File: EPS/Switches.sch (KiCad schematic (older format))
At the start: 13 parts, among them Q13 PMOS_IN, Q14 Q_NMOS_GSD, Q15 PMOS_IN, Q16 PMOS_OUT1, Q17 PMOS_OUT2, Q18 NMOS_MCU

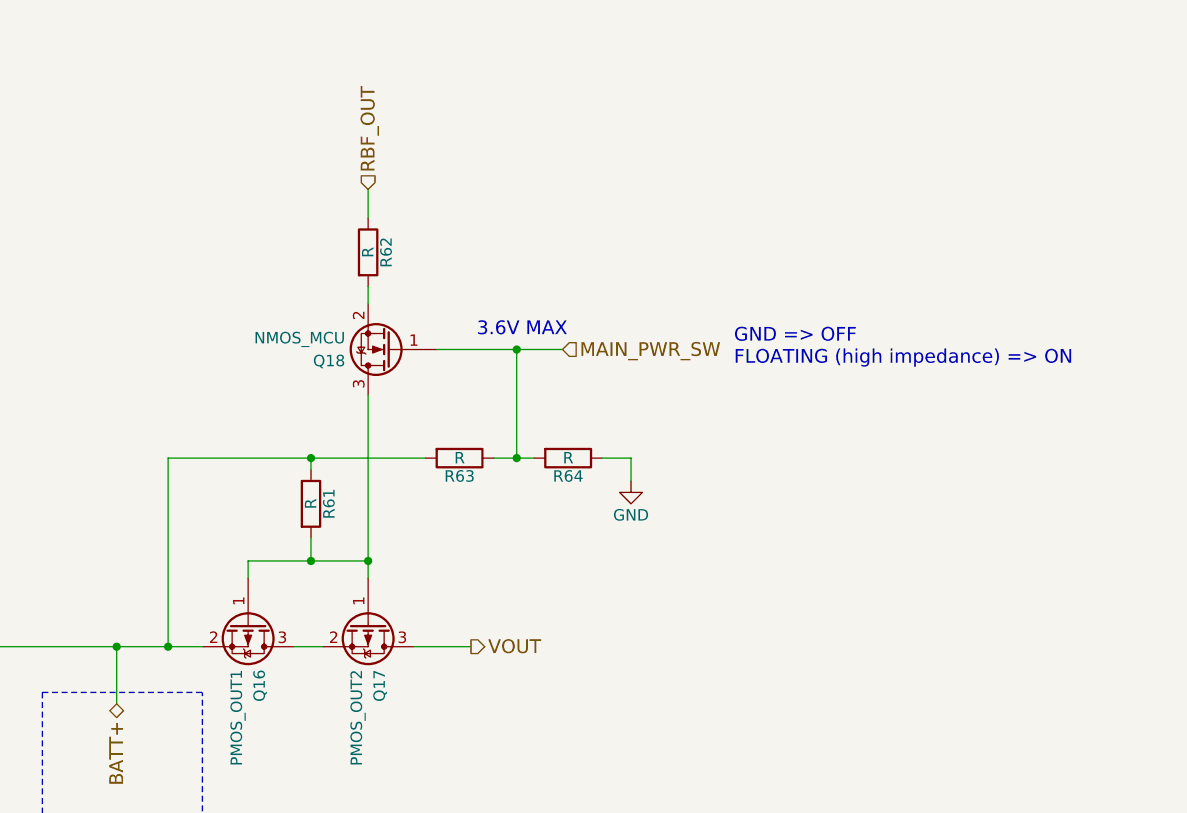
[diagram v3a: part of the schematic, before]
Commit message: PCB updated
Added testpoints and updated PCB
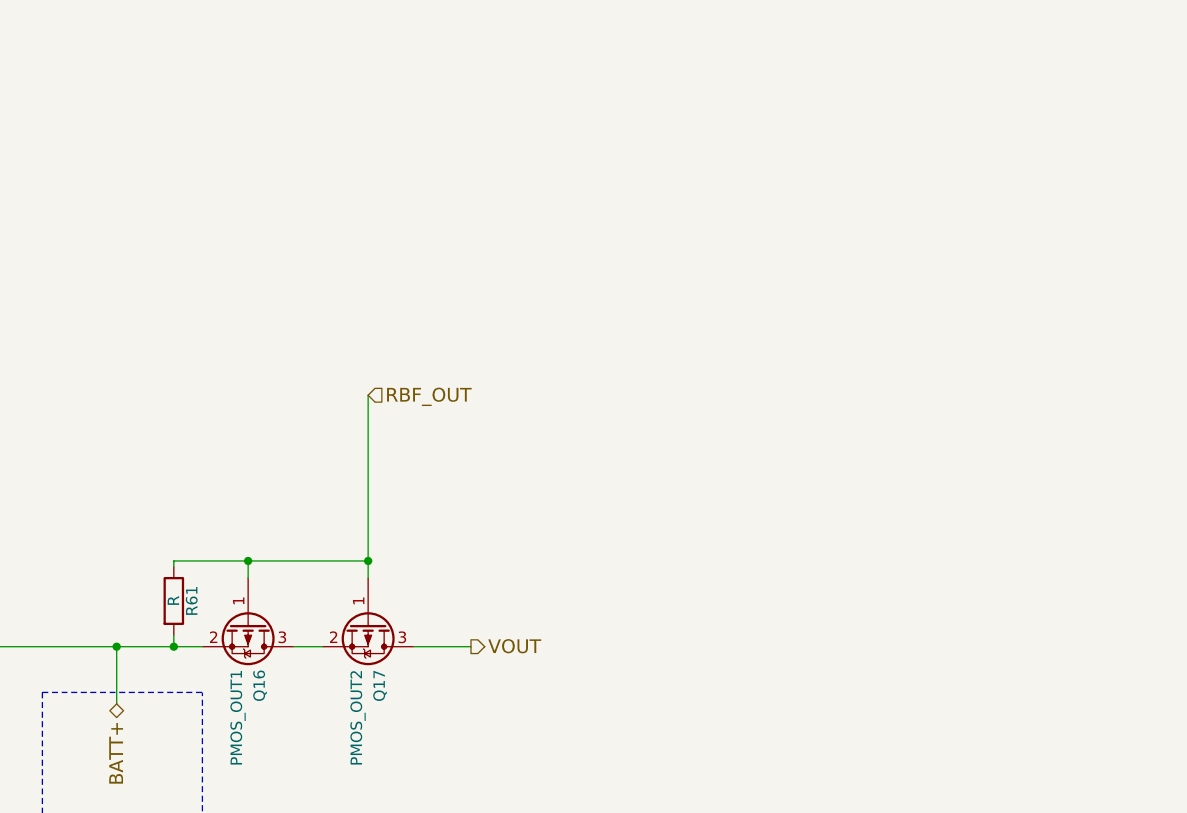
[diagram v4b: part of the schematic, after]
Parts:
- removed Q18: NMOS_MCU, TO_SOT_Packages_SMD:SOT-23, symbol Q_NMOS_GSD
- removed R62, R63, R64: R, Resistors_SMD:R_0603, symbol R
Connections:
- net BATT+: now also R61.2; no longer R61.1
- net RBF_OUT: now also Q16.1 (G), Q17.1 (G), R61.1
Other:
- note removed: "3.6V MAX"
- note removed: "GND => OFF\nFLOATING (high impedance) => ON"
- moved on the sheet: R61
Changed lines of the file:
@@
 Sheet 14 14
 Title "Switches"
-Date "2018-02-15"
+Date "2018-03-05"
 Rev "R1"
 Comp ""
@@
 $EndComp
 $Comp
-L R R64
-U 1 1 5A894583
-P 8300 2625
-F 0 "R64" V 8380 2625 50  0000 C CNN
-F 1 "R" V 8300 2625 50  0000 C CNN
-F 2 "Resistors_SMD:R_0603" V 8230 2625 50  0001 C CNN
-F 3 "" H 8300 2625 50  0001 C CNN
-	1    8300 2625
-	0    1    1    0
-$EndComp
-$Comp
 L R R61
 U 1 1 5A89460C
-P 7175 2825
-F 0 "R61" V 7255 2825 50  0000 C CNN
-F 1 "R" V 7175 2825 50  0000 C CNN
-F 2 "Resistors_SMD:R_0603" V 7105 2825 50  0001 C CNN
-F 3 "" H 7175 2825 50  0001 C CNN
-	1    7175 2825
-	1    0    0    -1
-$EndComp
-$Comp
-L R R62
-U 1 1 5A8946B5
-P 7425 1725
-F 0 "R62" V 7505 1725 50  0000 C CNN
-F 1 "R" V 7425 1725 50  0000 C CNN
-F 2 "Resistors_SMD:R_0603" V 7355 1725 50  0001 C CNN
-F 3 "" H 7425 1725 50  0001 C CNN
-	1    7425 1725
-	1    0    0    -1
-$EndComp
-$Comp
-L R R63
-U 1 1 5A894711
-P 7825 2625
-F 0 "R63" V 7905 2625 50  0000 C CNN
-F 1 "R" V 7825 2625 50  0000 C CNN
-F 2 "Resistors_SMD:R_0603" V 7755 2625 50  0001 C CNN
-F 3 "" H 7825 2625 50  0001 C CNN
-	1    7825 2625
-	0    1    1    0
-$EndComp
-$Comp
-L GND #PWR0157
-U 1 1 5A89494F
-P 8575 2725
-F 0 "#PWR0157" H 8575 2475 50  0001 C CNN
-F 1 "GND" H 8575 2575 50  0000 C CNN
-F 2 "" H 8575 2725 50  0001 C CNN
-F 3 "" H 8575 2725 50  0001 C CNN
-	1    8575 2725
+P 6575 3250
+F 0 "R61" V 6655 3250 50  0000 C CNN
+F 1 "R" V 6575 3250 50  0000 C CNN
+F 2 "Resistors_SMD:R_0603" V 6505 3250 50  0001 C CNN
+F 3 "" H 6575 3250 50  0001 C CNN
+	1    6575 3250
 	1    0    0    -1
 $EndComp
@@
 	0    1    1    0
 $EndComp
-Wire Wire Line
-	7100 3450 7225 3450
 Text HLabel 6325 3700 3    60   BiDi ~ 0
 BATT+
 Text HLabel 6325 4700 1    60   BiDi ~ 0
 BATT-
-Wire Notes Line
-	6000 3650 6700 3650
-Wire Notes Line
-	6000 3650 6000 4800
-Wire Notes Line
-	6000 4800 6700 4800
-Wire Notes Line
-	6700 4800 6700 3650
-Wire Wire Line
-	6325 4700 6325 4900
-Wire Wire Line
-	4850 3450 6700 3450
-Wire Wire Line
-	6325 3700 6325 3450
-Connection ~ 6325 3450
-Wire Wire Line
-	6900 3150 6900 3075
-Wire Wire Line
-	6900 3075 7425 3075
-Wire Wire Line
-	7175 3075 7175 2975
-Wire Wire Line
-	7425 2350 7425 3150
-Connection ~ 7175 3075
-Wire Wire Line
-	6550 3450 6550 2625
-Wire Wire Line
-	6550 2625 7675 2625
-Wire Wire Line
-	7175 2625 7175 2675
-Connection ~ 6550 3450
-$Comp
-L Q_NMOS_GSD Q18
-U 1 1 5A8DFF70
-P 7525 2150
-F 0 "Q18" H 7725 2200 50  0000 L CNN
-F 1 "NMOS_MCU" H 7725 2100 50  0000 L CNN
-F 2 "TO_SOT_Packages_SMD:SOT-23" H 7725 2250 50  0001 C CNN
-F 3 "" H 7525 2150 50  0001 C CNN
-	1    7525 2150
-	-1   0    0    1
-$EndComp
-Connection ~ 7425 3075
-Wire Wire Line
-	7425 1950 7425 1875
-Connection ~ 7175 2625
-Wire Wire Line
-	7975 2625 8150 2625
-Wire Wire Line
-	8450 2625 8575 2625
-Wire Wire Line
-	8575 2625 8575 2725
 Text HLabel 7875 3450 2    60   Output ~ 0
 VOUT
-Wire Wire Line
-	7875 3450 7625 3450
-Wire Wire Line
-	7725 2150 8275 2150
-Wire Wire Line
-	8075 2150 8075 2625
-Connection ~ 8075 2625
-Text HLabel 7425 1450 1    60   Input ~ 0
-RBF_OUT
-Wire Wire Line
-	7425 1450 7425 1575
-Text HLabel 8275 2150 2    60   Input ~ 0
-MAIN_PWR_SW
 Text Notes 850  1000 0    60   ~ 0
 RBF pins:\n-GND before flight (OFF)\n-FLOATING when activated (ON)
@@
 Text Notes 850  1550 0    60   ~ 0
 Choose correct resistor values\n
-Connection ~ 8075 2150
 Text Notes 850  1825 0    60   ~ 0
 All MOSFETs are encoded as\n(1) gate, (2) source, (3) drain
-Text Notes 7900 2100 0    60   ~ 0
-3.6V MAX
-Text Notes 9025 2225 0    60   ~ 0
-GND => OFF\nFLOATING (high impedance) => ON
 $Comp
 L Q_PMOS_GSD Q15
@@
 	0    -1   -1   0
 $EndComp
-Wire Wire Line
-	4400 3450 4450 3450
-Wire Wire Line
-	3675 3450 4000 3450
-Wire Wire Line
-	3875 3450 3875 3500
-Connection ~ 3875 3450
-Wire Wire Line
-	3875 3850 4650 3850
-Wire Wire Line
-	4200 3850 4200 3750
-Wire Wire Line
-	4650 3850 4650 3750
-Connection ~ 4200 3850
-Wire Wire Line
-	4425 3850 4425 4175
-Connection ~ 4425 3850
 $Comp
 L Q_NMOS_GSD Q14
@@
 $EndComp
 $Comp
-L GND #PWR0158
+L GND #PWR0155
 U 1 1 5A9069CB
 P 4425 4775
-F 0 "#PWR0158" H 4425 4525 50  0001 C CNN
+F 0 "#PWR0155" H 4425 4525 50  0001 C CNN
 F 1 "GND" H 4425 4625 50  0000 C CNN
 F 2 "" H 4425 4775 50  0001 C CNN
@@
 	1    0    0    -1
 $EndComp
-Wire Wire Line
-	4425 4775 4425 4575
 $Comp
 L R R58
@@
 	0    -1   -1   0
 $EndComp
-Wire Wire Line
-	3625 4375 4125 4375
-Connection ~ 4050 4375
-Wire Wire Line
-	3775 4575 3775 4375
-Connection ~ 3775 4375
 Text HLabel 3200 4375 0    60   Input ~ 0
 CHARGER_IN_SWITCH
-Wire Wire Line
-	3200 4375 3325 4375
 Text Notes 3375 4850 0    60   ~ 0
 GND = OFF\nFLOAT = ON
@@
 $EndComp
 Wire Wire Line
+	7100 3450 7225 3450
+Wire Notes Line
+	6000 3650 6700 3650
+Wire Notes Line
+	6000 3650 6000 4800
+Wire Notes Line
+	6000 4800 6700 4800
+Wire Notes Line
+	6700 4800 6700 3650
+Wire Wire Line
+	6325 4700 6325 4900
+Wire Wire Line
+	4850 3450 6700 3450
+Wire Wire Line
+	6325 3700 6325 3450
+Connection ~ 6325 3450
+Wire Wire Line
+	6900 3150 6900 3075
+Wire Wire Line
+	7425 2350 7425 3150
+Connection ~ 7425 3075
+Wire Wire Line
+	7875 3450 7625 3450
+Wire Wire Line
+	4400 3450 4450 3450
+Wire Wire Line
+	3675 3450 4000 3450
+Wire Wire Line
+	3875 3450 3875 3500
+Connection ~ 3875 3450
+Wire Wire Line
+	3875 3850 4650 3850
+Wire Wire Line
+	4200 3850 4200 3750
+Wire Wire Line
+	4650 3850 4650 3750
+Connection ~ 4200 3850
+Wire Wire Line
+	4425 3850 4425 4175
+Connection ~ 4425 3850
+Wire Wire Line
+	4425 4775 4425 4575
+Wire Wire Line
+	3625 4375 4125 4375
+Connection ~ 4050 4375
+Wire Wire Line
+	3775 4575 3775 4375
+Connection ~ 3775 4375
+Wire Wire Line
+	3200 4375 3325 4375
+Wire Wire Line
 	4050 4375 4050 4300
 Wire Wire Line
@@
 Wire Wire Line
 	3875 3800 3875 3850
+Wire Wire Line
+	6575 3400 6575 3450
+Connection ~ 6575 3450
+Wire Wire Line
+	6575 3075 6575 3100
+Connection ~ 6900 3075
+Text HLabel 7425 2350 2    60   Input ~ 0
+RBF_OUT
+Wire Wire Line
+	6575 3075 7425 3075
 $EndSCHEMATC
